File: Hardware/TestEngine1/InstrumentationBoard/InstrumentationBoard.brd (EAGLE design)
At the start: 162.2 x 80 mm, 109 parts, among them IC1 MAX31855, J1 1X2-3.5MM, Q1 MOSFET-NCHANNELBSS123LT1G, Q2 MOSFET-NCHANNELBSS123LT1G, Q3 MOSFET-NCHANNELBSS123LT1G, U1 BMP180

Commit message: work in progress in laying out and routing instrument board
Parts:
- removed C11: 0.33uF, SparkFun-Capacitors:0805
- removed C12: 0.1uF, SparkFun-Capacitors:0805
- removed D1: 1n4148, adafruit:SOD-323F
- removed D2: 1N4148, adafruit:SOD-323F
- removed JP20: (no value), SparkFun-Connectors:1X03
- removed JP21, JP22, JP23, JP24: M02PTH, SparkFun-Connectors:1X02
- removed R18: 10K, adafruit:R0805
- removed U$8: MC33269DTRK, RitLaunchInitiative:TO-252
- added JP133: (no value), SparkFun-Connectors:1X05
- added JP1777: M02PTH, SparkFun-Connectors:1X02
- added JP55: (no value), SparkFun-Connectors:1X04
- added R35: 10K, SparkFun-Resistors:0805
- added U$10: BOOSTER_PACK_CONNECTED, RitLaunchInitiative:TI_CONNECTED_BOOSTER
- C1, C2: device adafruit:C0805K -> SparkFun-Capacitors:0805
- JP11, JP14, JP15: value (none) -> M02PTH; device SparkFun-Connectors:1X03 -> SparkFun-Connectors:1X02
- JP12, JP5: value (none) -> M02PTH; device SparkFun-Connectors:1X04 -> SparkFun-Connectors:1X02
- JP13: value (none) -> M02PTH; device SparkFun-Connectors:1X05 -> SparkFun-Connectors:1X02
- JP17, JP18, JP9: value M02PTH -> (none); device SparkFun-Connectors:1X02 -> SparkFun-Connectors:1X03
- R1, R2, R8: value 10K -> 10k; device adafruit:R0805 -> SparkFun-Resistors:0805
- R10, R11, R30, R34, R9: device adafruit:R0805 -> SparkFun-Resistors:0805
- R12, R25: value 1.7k -> 10K
- R13, R26: value 3.3k -> 10K
- R14: value 68 -> 1.7k; device adafruit:R0805 -> SparkFun-Resistors:0805
- R15: value 0 -> 3.3k; device adafruit:R0805 -> SparkFun-Resistors:0805
- R16: value 0 -> 1.7k; device adafruit:R0805 -> SparkFun-Resistors:0805
- R17: value 10K -> 3.3k; device adafruit:R0805 -> SparkFun-Resistors:0805
- R19: value 10K -> 9k; device adafruit:R0805 -> SparkFun-Resistors:0805
- R20: value 10K -> 3k; device adafruit:R0805 -> SparkFun-Resistors:0805
- R21: value 10K -> 100; device adafruit:R0805 -> SparkFun-Resistors:0805
- R22: value 9k -> 220; device adafruit:R0805 -> SparkFun-Resistors:0805
- R23: value 3k -> 680; device adafruit:R0805 -> SparkFun-Resistors:0805
- R24, R31, R32: value 10k -> 10K
- R27: value 100 -> 68; device adafruit:R0805 -> SparkFun-Resistors:0805
- R28: value 220 -> 0; device adafruit:R0805 -> SparkFun-Resistors:0805
- R29: value 680 -> 0; device adafruit:R0805 -> SparkFun-Resistors:0805
- R33: value 10k -> 1K
- R7: value 1K -> 10k; device adafruit:R0805 -> SparkFun-Resistors:0805
- moved R34 548.7 mm to (92.7, 59.7)
- moved R33 527.0 mm to (92.7, 48.3)
- moved D10 500.4 mm to (62.2, 68.6), turned to 90 degrees
- moved JP25 497.7 mm to (72.4, 20.3), turned to 180 degrees
- moved R32 497.2 mm to (72.4, 36.8)
- moved R31 482.1 mm to (71.1, 31.8), turned to 90 degrees
- moved U$9 480.5 mm to (55.9, 67.3)
- moved R30 458.6 mm to (67.3, 30.5)
- moved D8 440.8 mm to (41.9, 35.6), turned to 90 degrees
- moved R29 439.6 mm to (38.1, 45.1)
- moved D7 438.6 mm to (44.5, 35.6), turned to 90 degrees
- moved R28 437.4 mm to (38.1, 48.9)
- moved R27 430.0 mm to (38.1, 47.0)
- moved C19 417.1 mm to (63.5, 34.3), turned to 180 degrees
- moved D9 416.1 mm to (39.4, 35.6), turned to 90 degrees
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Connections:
- removed net SCLK: D1.C
- removed net THERMOCOUPLE_CS: D2.C
- new net KEYSWITCH_1: JP25.1, R31.1
- net +3V3: now also JP1777.2, JP5.2, JP6.2, JP7.2, JP8.2, R21.1, R28.1, R29.1, R34.1, R35.1, U$10.3.3V, U$10.3.3V1; no longer JP12.2, JP17.2, JP18.2, JP22.2, JP23.2, JP24.2, R1.1, R14.1, R15.1, R16.1, R2.1
- net 12V: now also JP11.2, JP12.2, JP13.2, JP133.5, JP14.2, JP15.2, R19.1, R23.1; no longer C11.1, JP12.4, JP13.5, JP21.2, JP6.2, JP7.2, JP8.2, JP9.2, R22.1, R29.1, U$8.3
- net 5V: now also JP17.2, JP18.2, JP19.2, JP9.1, R22.1, U$10.5V, U$10.5V1; no longer C12.1, JP12.3, JP14.2, JP15.2, JP19.1, JP20.2, R28.1, U$8.2
- net BATTVOLTAGE: now also R19.2, R20.1, U$10.AIN19/PK3; no longer R22.2, R23.1
- net BLUE: now also R26.1; no longer R17.1
- net CS: now also R35.2; no longer D2.A, R2.2
- net FET1: now also R9.1, U$10.T0CCP1/PL5; no longer R8.1
- net FET2: now also R10.1, U$10.PL0; no longer R9.1
- net FET3: now also R11.1, U$10.PL1; no longer R10.1
- net FET4: now also R12.1, U$10.PL2; no longer R11.1
- net FET5: now also R13.1, U$10.PL3; no longer R30.1
- net GND: now also JP133.3, JP133.4, JP17.3, JP18.3, JP55.4, JP9.3, R1.1, R12.2, R13.2, R15.1, R17.1, R2.1, R24.2, R25.2, R26.2, R31.2, R32.2, R7.1, R8.1, U$10.GND, U$10.GND1, U$10.GND2, U$10.GND3; no longer JP11.1, JP12.1, JP13.3, JP13.4, JP14.3, JP15.3, JP20.3, JP5.4, R13.1, R17.2, R18.2, R19.2, R21.2, R23.2, R24.1, R26.1, R31.1, R32.1, R33.1, R34.2, R8.2
- net GREEN: now also R25.1; no longer R18.1
- net LOADCELL: now also U$10.AIN18/PK2
- net N$10: now also R28.2; no longer R15.2
- net N$11: now also JP55.1; no longer JP5.1
- net N$12: no longer C11.2, C12.2, U$8.1
- net N$13: now also R33.2; no longer R7.2
- net N$14: now also R33.1; no longer R7.1
- net N$15: now also R29.2; no longer R16.2
- net N$16: now also JP55.2; no longer JP5.2
- net N$17: now also JP14.1; no longer JP9.1
- net N$18: now also JP11.1; no longer JP6.1
- net N$19: now also JP12.1; no longer JP7.1
- net N$2: now also JP9.2, R14.2; no longer JP10.2, R12.2
- net N$20: now also JP55.3; no longer JP5.3
- net N$21: now also JP10.2, R16.2; no longer JP19.2, R25.2
- net N$22: now also JP13.1; no longer JP8.1
- net N$23: now also R22.2; no longer R28.2
- net N$24: now also R21.2; no longer R27.2
- net N$25: now also R23.2; no longer R29.2
- net N$26: now also JP15.1; no longer JP21.1
- net N$9: now also R27.2; no longer R14.2
- net PSI_1: now also R14.1, R15.2, U$10.AIN16/PK0; no longer R12.1, R13.2
- net PSI_2: now also R16.1, R17.2, U$10.AIN17/PK1; no longer R25.1, R26.2
- net PWM_1: now also JP16.1, U$10.M0PWM1/PF1; no longer JP14.1
- net PWM_2: now also JP17.1, U$10.M0PWM2/PF2; no longer JP15.1
- net PWM_3: now also JP18.1, U$10.M0PWM3/PF3; no longer JP16.1
- net PWM_4: now also JP19.1, U$10.M0PWM4/PG0; no longer JP20.1
- net RED: now also R24.1; no longer R19.1
- net SCK: now also R34.2; no longer D1.A, R1.2
- net SCL: now also JP133.2, U$10.I2C0SCL/PB2; no longer JP11.2, JP13.2
- net SDA: now also JP133.1, U$10.I2C0SDA/PB3; no longer JP11.3, JP13.1
- net SW_1: now also R32.1; no longer R20.1
- net TILTSWITCH_1: now also JP1777.1, R30.1; no longer JP17.1, JP25.1, R21.1, R34.1
- net TR1: now also R1.2; no longer R3.2
- net TR2: now also R2.2; no longer R4.2
- net TR3: now also R3.2; no longer R5.2
- net TR4: now also R4.2; no longer R6.2
- net TR5: now also JP5.1, R5.2; no longer JP18.1, R24.2
- net TR6: now also JP6.1, R6.2, U$10.AIN13/PD2; no longer JP22.1, R31.2
- net TR7: now also JP7.1, R7.2, U$10.AIN10/PB4; no longer JP23.1, R32.2
- net TR8: now also JP8.1, R8.2, U$10.AIN11/PB5; no longer JP24.1, R33.2
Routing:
- added copper zone on layer 1, net GND
- added copper zone on layer 16, net GND
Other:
- board size 162.2 x 80 mm -> 107.6 x 80 mm

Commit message: work in progress on pcb's
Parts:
- added JP20: (no value), SparkFun-Connectors:1X03
- added R18: 1.7k, SparkFun-Resistors:0805
- added R36: 3.3k, SparkFun-Resistors:0805
- moved JP1777 263.0 mm to (25.4, 17.8), turned to 180 degrees
- moved D9 26.4 mm to (61.0, 20.3), turned to 0 degrees
- moved D7 26.2 mm to (61.0, 15.2), turned to 0 degrees
- moved D8 26.1 mm to (61.0, 17.8), turned to 0 degrees
- moved JP25 23.3 mm to (52.1, 31.8), turned to 90 degrees
- moved R23 19.4 mm to (55.9, 20.3), turned to 0 degrees
- moved C4 19.2 mm to (47.6, 3.81)
- moved R22 19.1 mm to (55.9, 15.2), turned to 0 degrees
- moved R21 18.9 mm to (55.9, 17.8), turned to 0 degrees
- moved C5 14.4 mm to (40.6, 11.4), turned to 270 degrees
- moved U$3 8.52 mm to (48.3, 22.9), turned to 270 degrees
- moved R17 8.28 mm to (4.45, 45.1), turned to 180 degrees
- moved R16 1.91 mm to (3.81, 42.5), turned to 270 degrees
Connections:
- new net N$27: JP20.2, R18.2
- new net PSI_3: R18.1, R36.2, U$10.AIN18/PK2
- net 5V: now also JP20.1
- net BATTVOLTAGE: now also U$10.PA6; no longer U$10.AIN19/PK3
- net BLUE: now also U$10.M0PWM7/PK5
- net CS: now also U$10.PQ1
- net GND: now also JP20.3, R36.1
- net GREEN: now also U$10.M0PWM6/PK4
- net KEYSWITCH_1: now also U$10.PH1
- net LOADCELL: now also U$10.AIN19/PK3; no longer U$10.AIN18/PK2
- net MISO: now also U$10.SSI3RX/PQ3
- net RED: now also U$10.M0PWM5/PG1
- net SCK: now also U$10.SSI3CLK/PQ0
- net SW_1: now also U$10.PK6
- net TILTSWITCH_1: now also U$10.PH0
- net TR1: now also U$10.AIN3/PE0
- net TR2: now also U$10.AIN2/PE1
- net TR3: now also U$10.AIN1/PE2
- net TR4: now also U$10.AIN0/PE3
- net TR5: now also U$10.AIN4/PD7

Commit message: power traces being layed out
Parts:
- moved S1 285.1 mm to (36.8, 31.8), turned to 270 degrees
- moved JP3 77.3 mm to (17.8, 22.9)
- moved JP5 77.3 mm to (22.9, 22.9)
- moved JP7 77.3 mm to (27.9, 22.9)
- moved R3 77.3 mm to (17.8, 19.1)
- moved R5 77.3 mm to (22.9, 19.1)
- moved R7 77.3 mm to (27.9, 19.1)
- moved JP2 77.3 mm to (15.2, 22.9)
- moved JP4 77.3 mm to (20.3, 22.9)
- moved JP6 77.3 mm to (25.4, 22.9)
- moved R2 77.3 mm to (15.2, 19.1)
- moved R4 77.3 mm to (20.3, 19.1)
- moved R6 77.3 mm to (25.4, 19.1)
- moved JP1 77.3 mm to (12.7, 22.9)
- moved JP8 77.3 mm to (30.5, 22.9)
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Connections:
- net N$4: now also IC1.3; no longer IC1.2
- net N$6: now also IC1.2; no longer IC1.3
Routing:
- net 12V: track 0.00 -> 68.1 mm
- net FET3: track 0.00 -> 42.9 mm
- net 5V: track 0.00 -> 36.3 mm
- net FET1: track 0.00 -> 29.2 mm, vias 0 -> 1
- net FET4: track 0.00 -> 27.2 mm
- net N$18: track 0.00 -> 13.7 mm
- net N$17: track 0.00 -> 13.0 mm
- net N$26: track 0.00 -> 13.0 mm
- net N$22: track 0.00 -> 13.0 mm
- net N$19: track 0.00 -> 12.8 mm
- net N$12: track 0.00 -> 12.2 mm
- net FET5: track 0.00 -> 12.2 mm
- net +3V3: track 0.00 -> 8.58 mm
- net PWM_1: track 0.00 -> 8.15 mm
- net PWM_4: track 0.00 -> 8.15 mm
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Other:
- board size 107.6 x 80 mm -> 105.1 x 80 mm

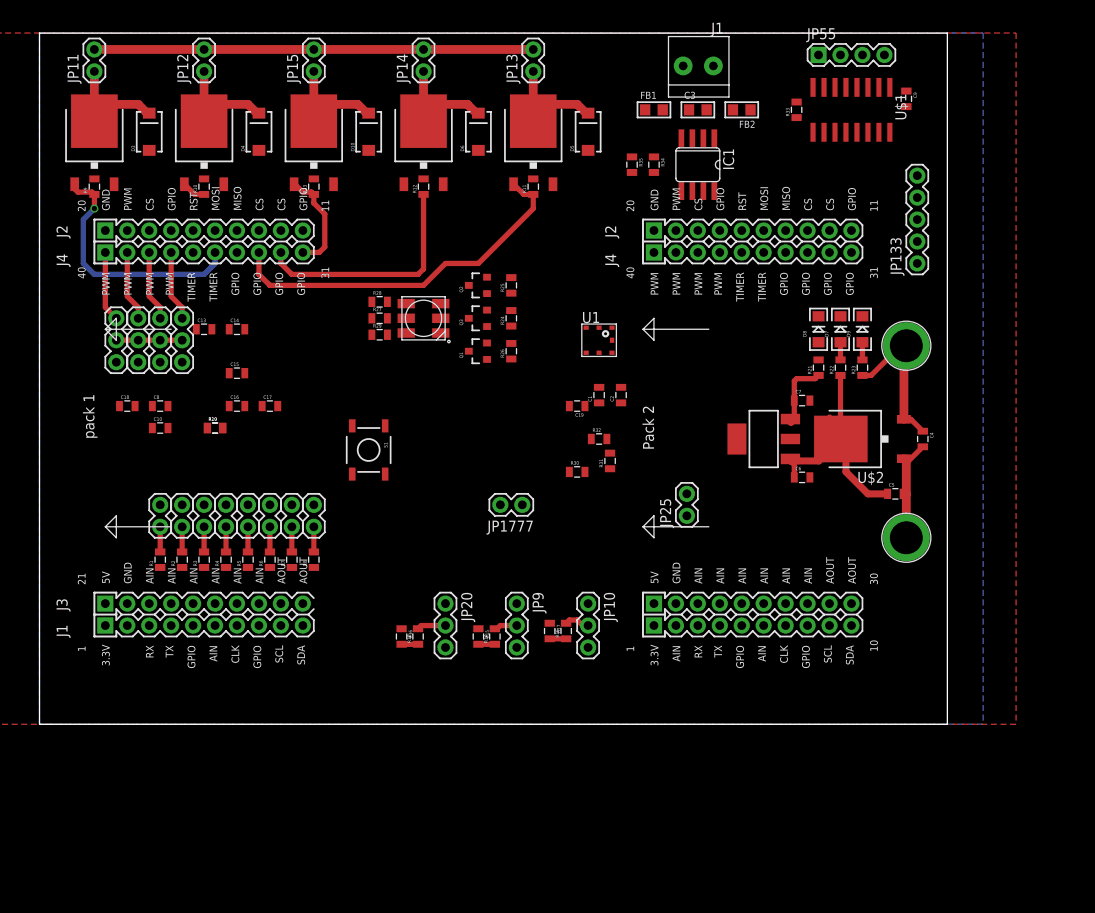
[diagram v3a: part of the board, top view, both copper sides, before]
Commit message: majority of power and analog busses layed out
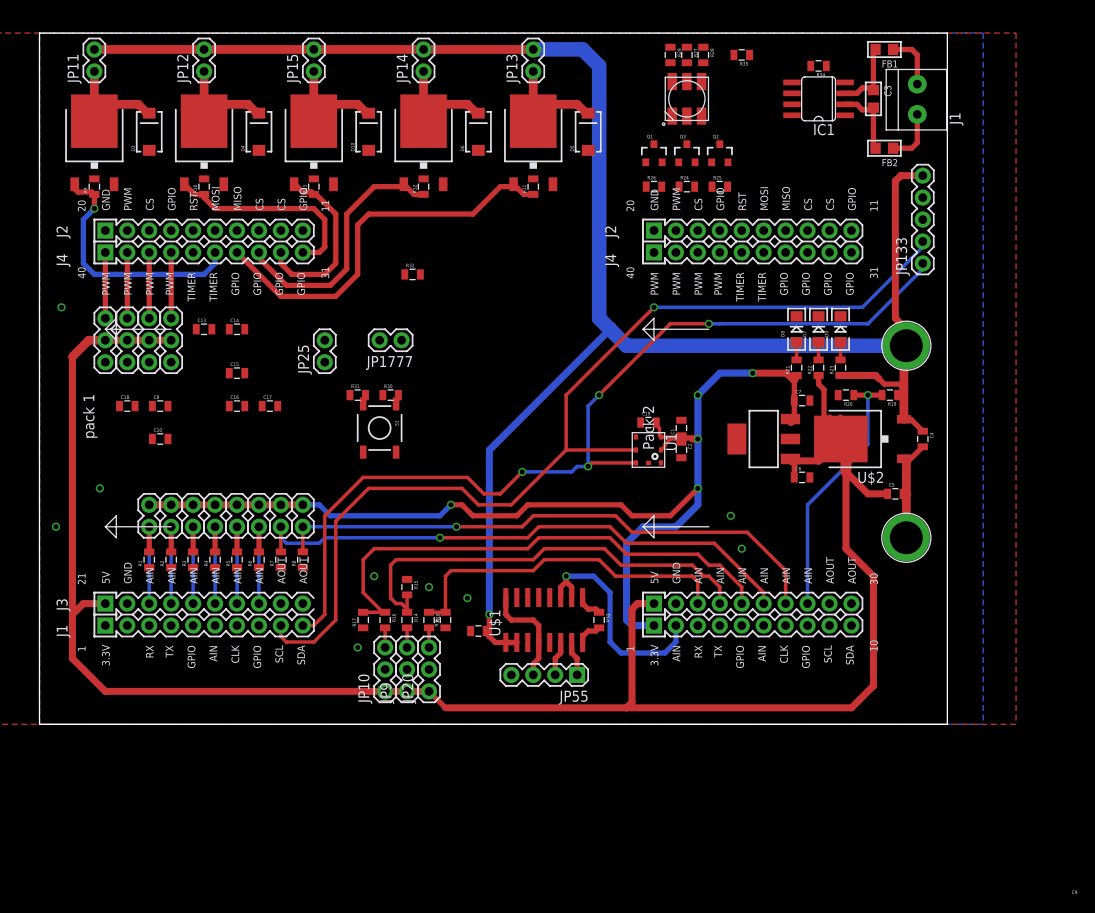
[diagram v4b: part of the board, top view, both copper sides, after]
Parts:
- moved C9 79.0 mm to (49.5, 10.8), turned to 180 degrees
- moved R19 78.2 mm to (97.2, 38.1), turned to 180 degrees
- moved JP55 77.0 mm to (61.0, 5.71), turned to 180 degrees
- moved R20 73.1 mm to (92.1, 38.1), turned to 180 degrees
- moved U$1 68.9 mm to (57.1, 12.1), turned to 0 degrees
- moved R33 63.3 mm to (63.5, 12.1), turned to 270 degrees
- moved R28 47.1 mm to (75.6, 77.5), turned to 270 degrees
- moved R27 46.8 mm to (73.7, 77.5), turned to 270 degrees
- moved R29 46.7 mm to (71.8, 77.5), turned to 270 degrees
- moved JP25 45.5 mm to (31.8, 41.9)
- moved LED1 39.7 mm to (73.7, 72.4), turned to 270 degrees
- moved Q2 31.8 mm to (77.5, 66.0), turned to 0 degrees
- moved Q3 30.7 mm to (73.7, 66.0), turned to 0 degrees
- moved Q1 30.6 mm to (69.8, 66.0), turned to 0 degrees
- moved R31 30.2 mm to (35.6, 38.1), turned to 0 degrees
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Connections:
- net BATTVOLTAGE: now also U$10.AIN19/PK3; no longer U$10.PA6
- net FET2: now also U$10.PL3; no longer U$10.PL0
- net FET3: now also U$10.PL0; no longer U$10.PL1
- net FET4: now also U$10.PL1; no longer U$10.PL2
- net FET5: now also U$10.PL2; no longer U$10.PL3
- net GND: now also JP10.2, JP20.2, JP9.2; no longer JP10.3, JP20.3, JP9.3
- net LOADCELL: now also U$10.AIN13/PD2; no longer U$10.AIN19/PK3
- net N$2: now also JP9.3; no longer JP9.2
- net N$21: now also JP10.3; no longer JP10.2
- net N$27: now also JP20.3; no longer JP20.2
- net PSI_1: now also U$10.AIN11/PB5; no longer U$10.AIN16/PK0
- net PSI_2: now also U$10.AIN16/PK0; no longer U$10.AIN17/PK1
- net PSI_3: now also U$10.AIN10/PB4; no longer U$10.AIN18/PK2
- net TR6: now also U$10.PA6; no longer U$10.AIN13/PD2
- net TR7: now also U$10.AIN17/PK1; no longer U$10.AIN10/PB4
- net TR8: now also U$10.AIN18/PK2; no longer U$10.AIN11/PB5
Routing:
- net 5V: track 36.3 -> 230.1 mm
- net 12V: track 68.1 -> 216.7 mm, vias 0 -> 1
- net +3V3: track 8.58 -> 134.9 mm, vias 0 -> 5
- net SCL: track 0.00 -> 115.5 mm, vias 0 -> 1
- net SDA: track 0.00 -> 107.6 mm, vias 0 -> 4
- net TR8: track 2.91 -> 65.8 mm, vias 0 -> 1
- net TR7: track 2.91 -> 65.5 mm, vias 0 -> 1
- net PSI_2: track 1.91 -> 59.0 mm
- net PSI_1: track 1.91 -> 51.3 mm
- net PSI_3: track 1.91 -> 39.7 mm
- net BATTVOLTAGE: track 0.00 -> 30.3 mm, vias 0 -> 1
- net LOADCELL: track 0.00 -> 27.0 mm, vias 0 -> 1
- net FET2: track 2.77 -> 24.1 mm
- net N$20: track 0.00 -> 12.3 mm
- net TR6: track 2.91 -> 11.8 mm
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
